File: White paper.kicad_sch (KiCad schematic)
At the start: 7 parts, among them J1 Conn_Coaxial, J2 Conn_Coaxial

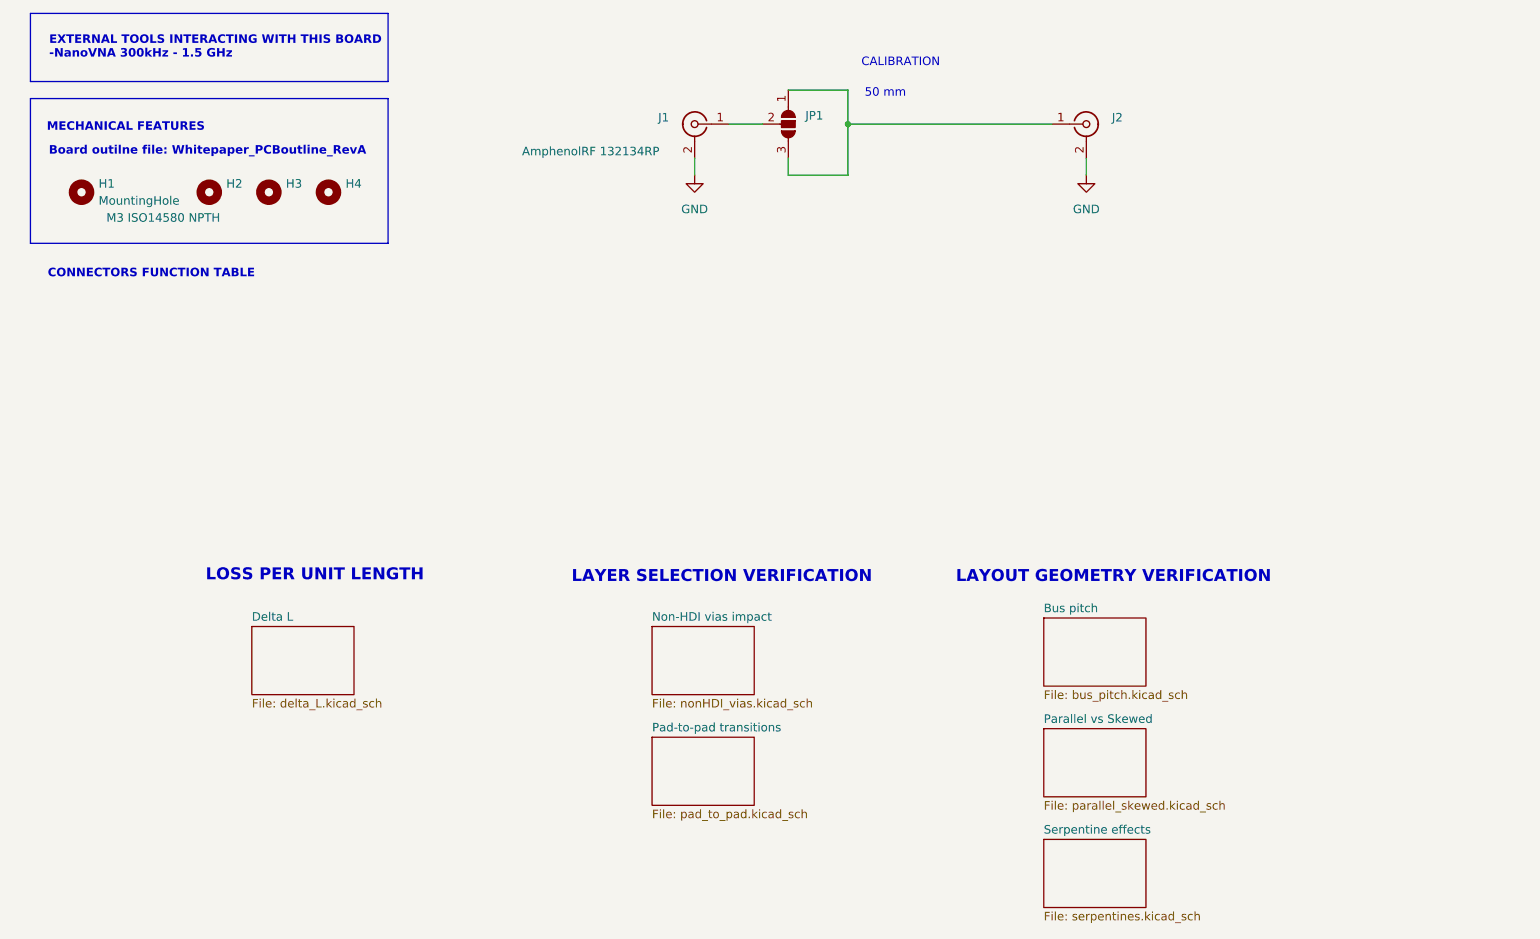
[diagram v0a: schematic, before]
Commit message: Rev B
Added 50R controlled Z, SOLT calibration and more reasonable tests
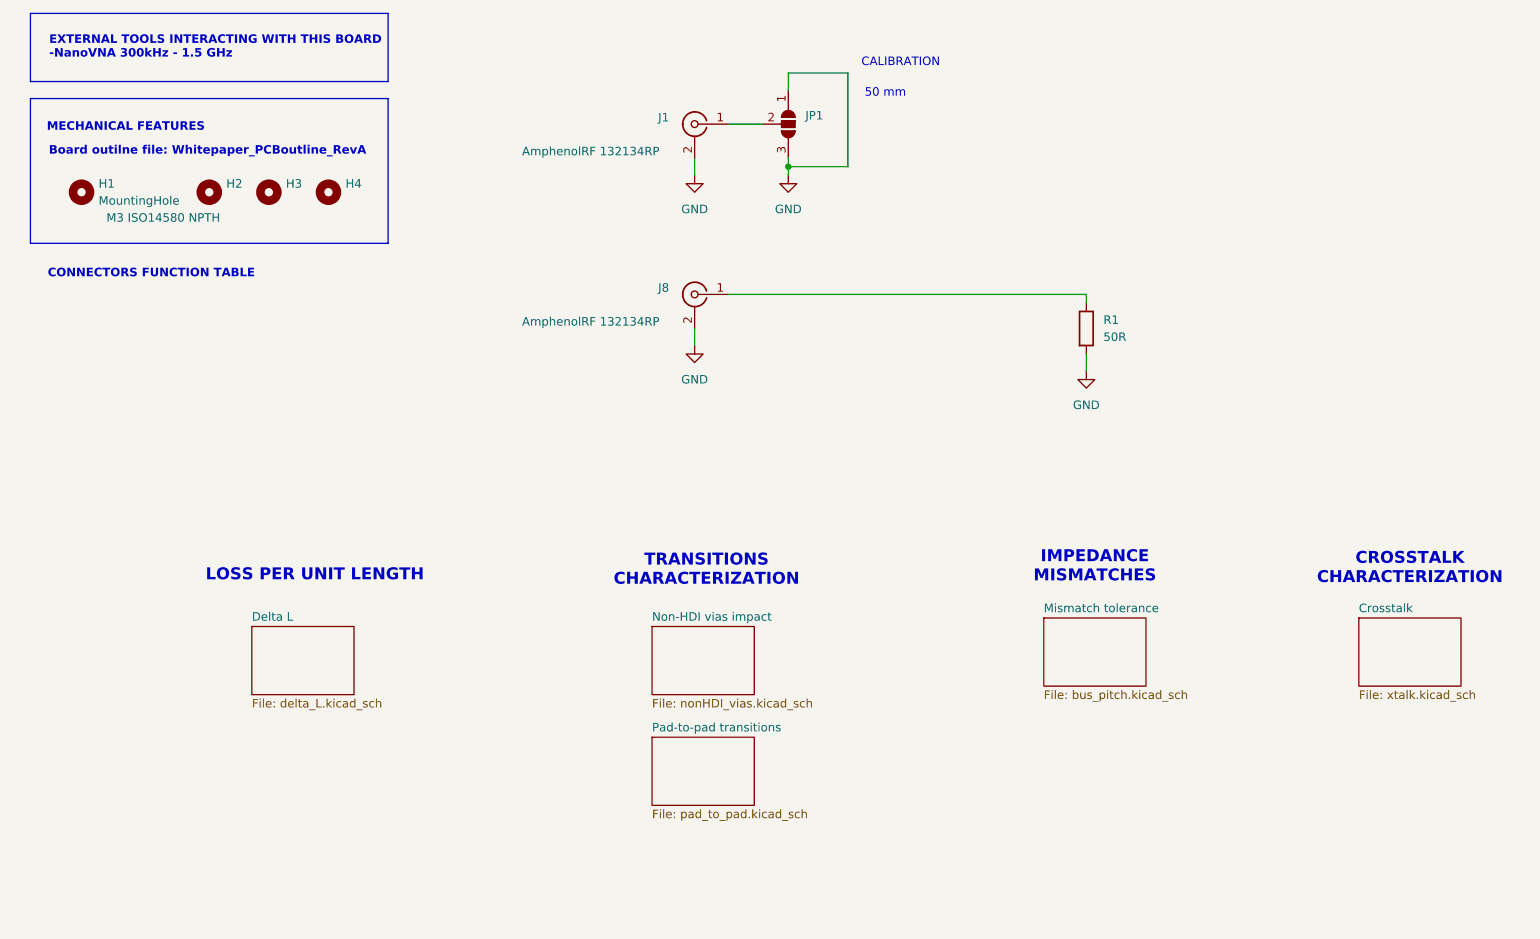
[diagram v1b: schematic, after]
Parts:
- removed J2: Conn_Coaxial, Library:SMA, symbol Connector:Conn_Coaxial
- added J8: Conn_Coaxial, Library:SMA, symbol Connector:Conn_Coaxial
- added R1: 50R, Resistor_SMD:R_0603_1608Metric, symbol Device:R
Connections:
- net GND: now also JP1.1 (A), JP1.3 (B), J8.2 (Ext), R1.2
- new net: J8.1 (In), R1.1
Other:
- sheet Bus pitch renamed Mismatch tolerance
- removed sheet Parallel vs Skewed
- removed sheet Serpentine effects
- added sheet Crosstalk (xtalk.kicad_sch)
- note added: "CROSSTALK CHARACTERIZATION"
- note added: "IMPEDANCE MISMATCHES"
- note added: "TRANSITIONS CHARACTERIZATION"
- note removed: "LAYER SELECTION VERIFICATION"
- note removed: "LAYOUT GEOMETRY VERIFICATION"
